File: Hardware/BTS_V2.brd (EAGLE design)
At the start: 113 x 79.4 mm, 64 parts, among them IC1 TPA3140D2PWP, IC2 BLK-MD-SPK-B, J1 SPKR_OUT, J2 RN52BoB_R, J3 RN52BoB_L, J4 TFT_CONNECTION, J6 HC-05, T3_2 TEENSY_3.1-3.2_DIL

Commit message: still tracking down issue
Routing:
- net PVCC: track 104.3 -> 100.7 mm
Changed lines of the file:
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@@
 <wire x1="86.78" y1="60.325" x2="83.185" y2="60.325" width="0.8128" layer="1"/>
 <wire x1="86.78" y1="66.04" x2="83.185" y2="66.04" width="0.8128" layer="1"/>
-<wire x1="80.882" y1="25.002" x2="77.885" y2="25.002" width="0.8128" layer="1"/>
+<wire x1="79.5782" y1="25.002" x2="77.885" y2="25.002" width="0.8128" layer="1"/>
 <wire x1="77.885" y1="25.002" x2="77.3688" y2="25.002" width="0.8128" layer="1"/>
-<via x="79.375" y="26.67" extent="1-16" drill="0.35"/>
-<wire x1="79.375" y1="26.67" x2="77.6986" y2="24.9936" width="0.8128" layer="16"/>
 <via x="68.072" y="24.9936" extent="1-16" drill="0.35"/>
 <wire x1="68.072" y1="24.9936" x2="69.9428" y2="24.9936" width="0.8128" layer="1"/>
 <wire x1="69.9428" y1="24.9936" x2="69.9512" y2="25.002" width="0.8128" layer="1"/>
-<wire x1="77.6986" y1="24.9936" x2="68.072" y2="24.9936" width="0.8128" layer="16"/>
 <wire x1="68.072" y1="24.9936" x2="66.675" y2="26.3906" width="0.8128" layer="1"/>
 <wire x1="66.675" y1="26.3906" x2="66.675" y2="27.09" width="0.8128" layer="1"/>
@@
 <wire x1="88.9" y1="71.12" x2="84.455" y2="71.12" width="0.8128" layer="1"/>
 <wire x1="83.185" y1="52.07" x2="83.185" y2="27.305" width="0.8128" layer="1"/>
-<wire x1="83.185" y1="27.305" x2="82.55" y2="26.67" width="0.8128" layer="1"/>
-<wire x1="82.55" y1="26.67" x2="80.882" y2="25.002" width="0.8128" layer="1"/>
-<wire x1="79.375" y1="26.67" x2="82.55" y2="26.67" width="0.8128" layer="1"/>
+<wire x1="83.185" y1="27.305" x2="80.882" y2="25.002" width="0.8128" layer="1"/>
 <contactref element="TP1" pad="TP"/>
 <wire x1="88.9" y1="71.12" x2="88.9" y2="69.215" width="0.8128" layer="1"/>
+<wire x1="80.882" y1="25.002" x2="79.5782" y2="25.002" width="0.8128" layer="1"/>
+<via x="79.5782" y="25.002" extent="1-16" drill="0.35"/>
+<wire x1="79.5782" y1="25.002" x2="79.5698" y2="24.9936" width="0.8128" layer="16"/>
+<wire x1="79.5698" y1="24.9936" x2="68.072" y2="24.9936" width="0.8128" layer="16"/>
 </signal>
 <signal name="N$3">

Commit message: still tracking down issue
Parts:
- added TP7, TP8: TPSPAD1-17, testpad:P1-17
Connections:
- net SPKR_R+: now also TP7.TP
- net SPKR_R-: now also TP8.TP
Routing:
- net GVDD: track 79.4 -> 49.3 mm, vias 4 -> 2
- net SPKR_R-: track 24.5 -> 33.5 mm, vias 0 -> 1
- net HC_UART_RX: track 157.4 -> 162.4 mm, vias 6 -> 7
- net GND: track 60.5 -> 62.2 mm
- net SHUTDOWN: track 6.55 -> 7.65 mm
- net MIC_BIAS: track 12.8 -> 13.7 mm
- net SPKR_R+: track 42.0 -> 42.9 mm
- net 3V3: track 257.8 -> 258.7 mm
- net GAIN: track 19.6 -> 18.9 mm
- net LED1: track 21.5 -> 22.1 mm
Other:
- board text added: "SPKR_R+"
- board text added: "SPKR_R-"

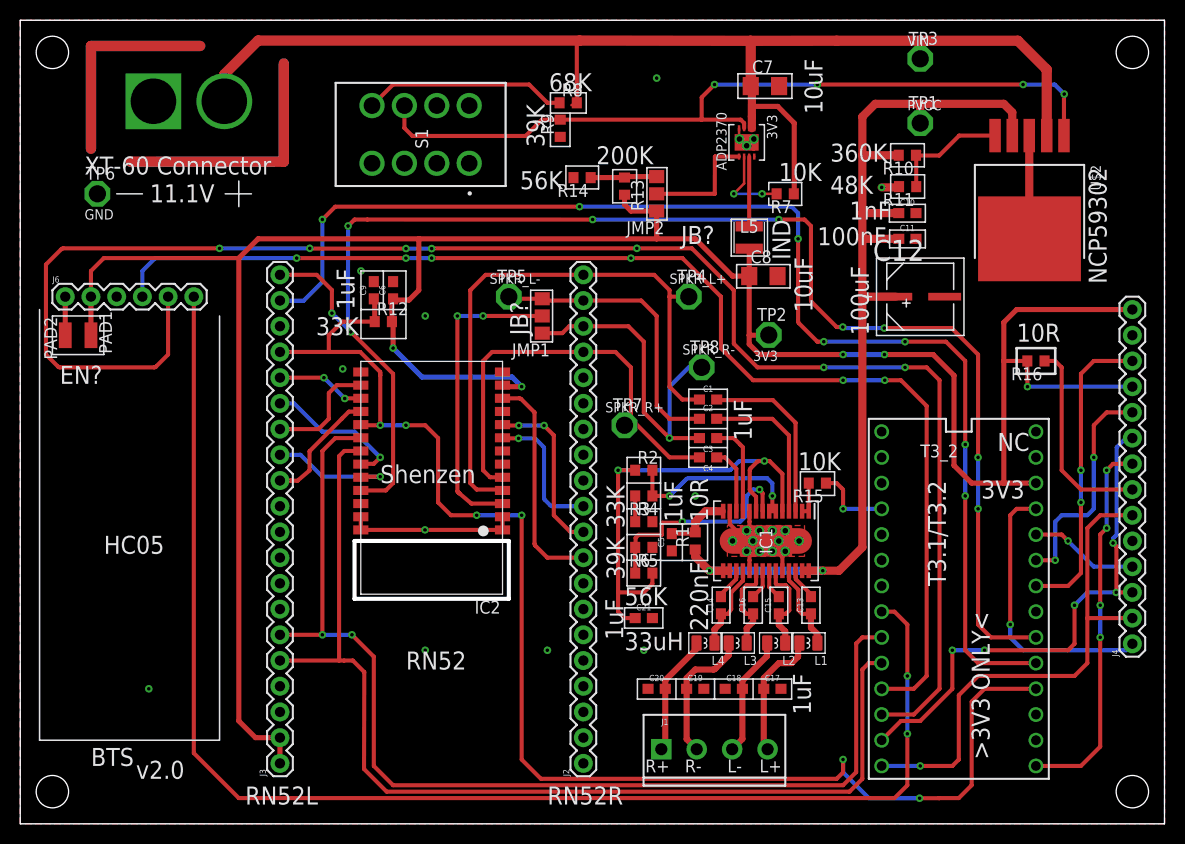
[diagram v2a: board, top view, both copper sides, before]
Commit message: Finally solved the issue - was a too large cap on output
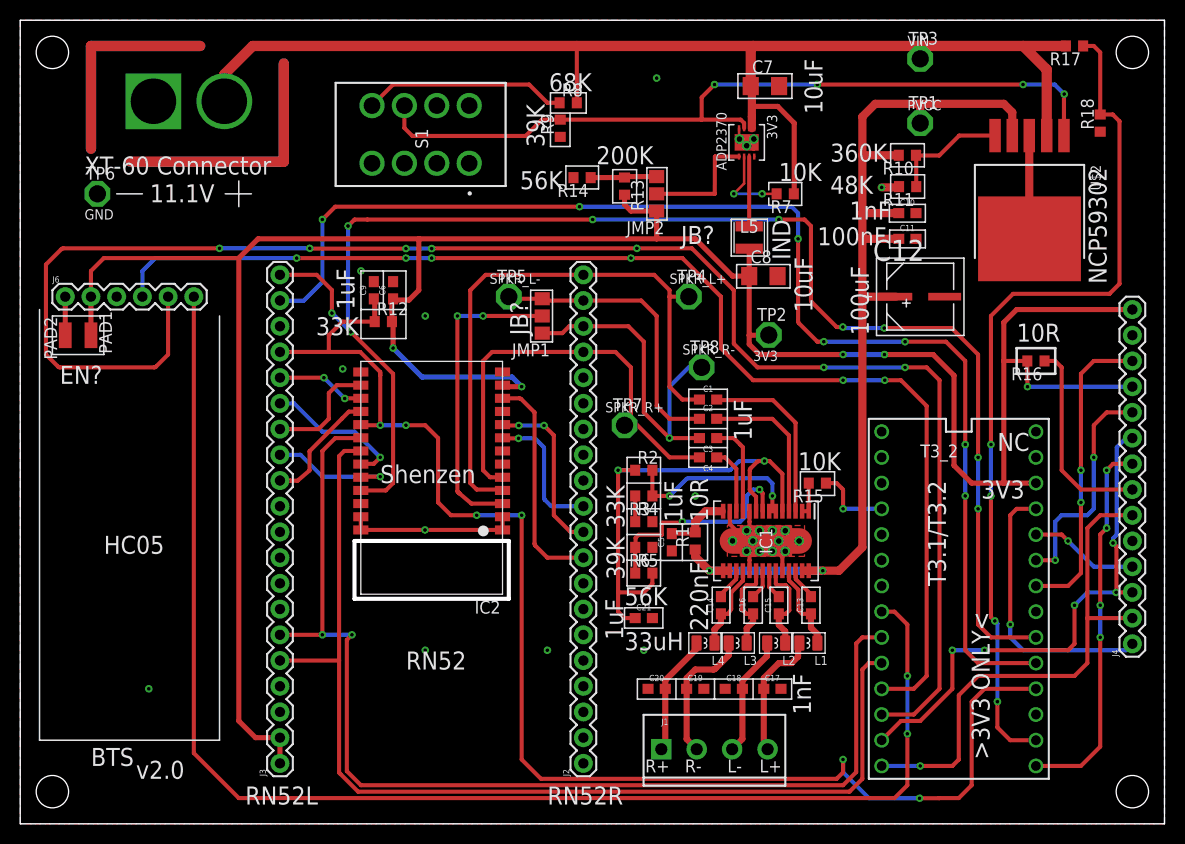
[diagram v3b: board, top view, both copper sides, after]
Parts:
- added R17: 360K, resistor:R0603
- added R18: 68K, resistor:R0603
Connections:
- removed net D14: T3_2.14/A0
- new net SAMP: R17.1, R18.2, T3_2.14/A0
- net GND: now also R18.1
- net VIN: now also R17.2
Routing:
- net SAMP: track 0.00 -> 85.6 mm, vias 0 -> 4
- net UART_TX: track 107.9 -> 110.2 mm
- net VIN: track 126.2 -> 125.1 mm
- net UART_RX: track 104.6 -> 105.4 mm
